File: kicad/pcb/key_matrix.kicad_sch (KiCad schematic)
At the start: 47 parts, among them SW1 EC_SW

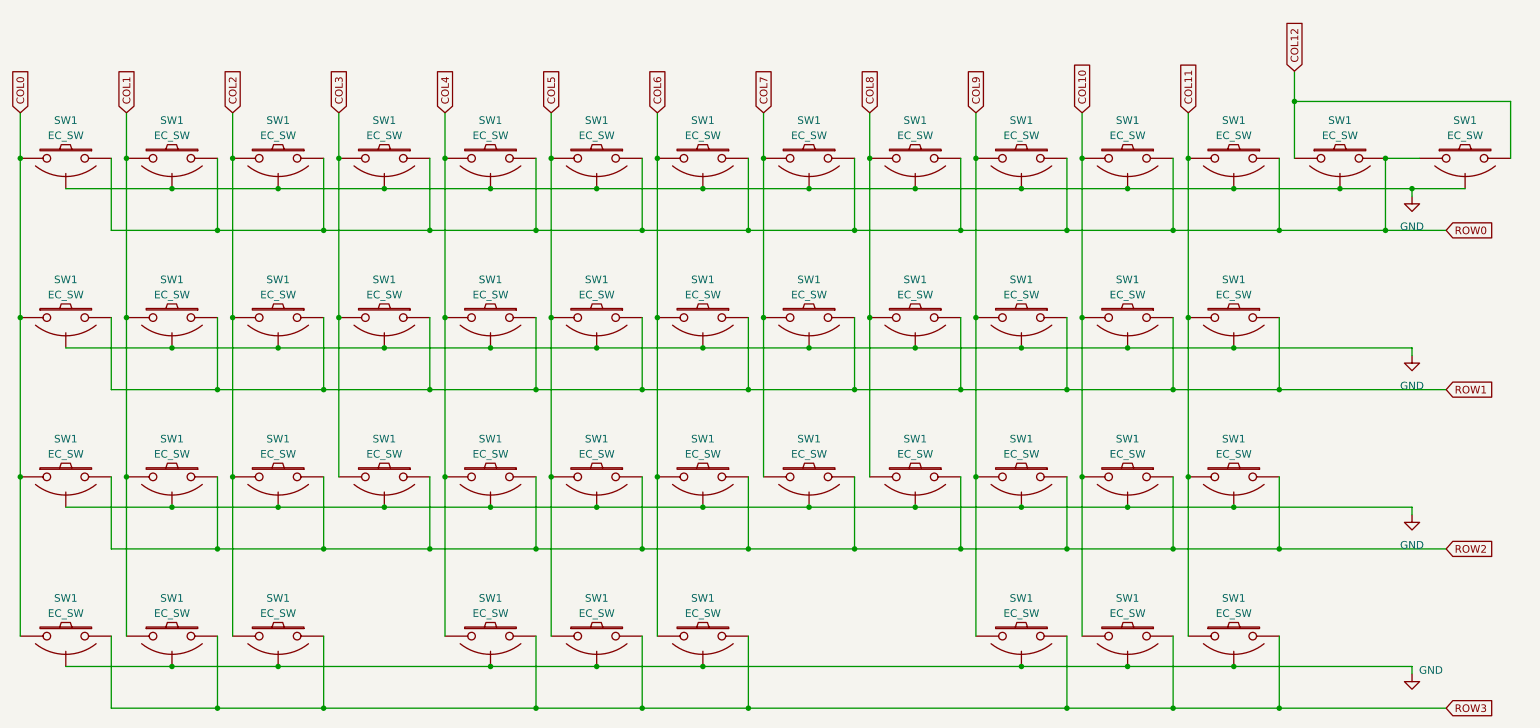
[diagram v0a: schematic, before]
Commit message: should be ok for proto order
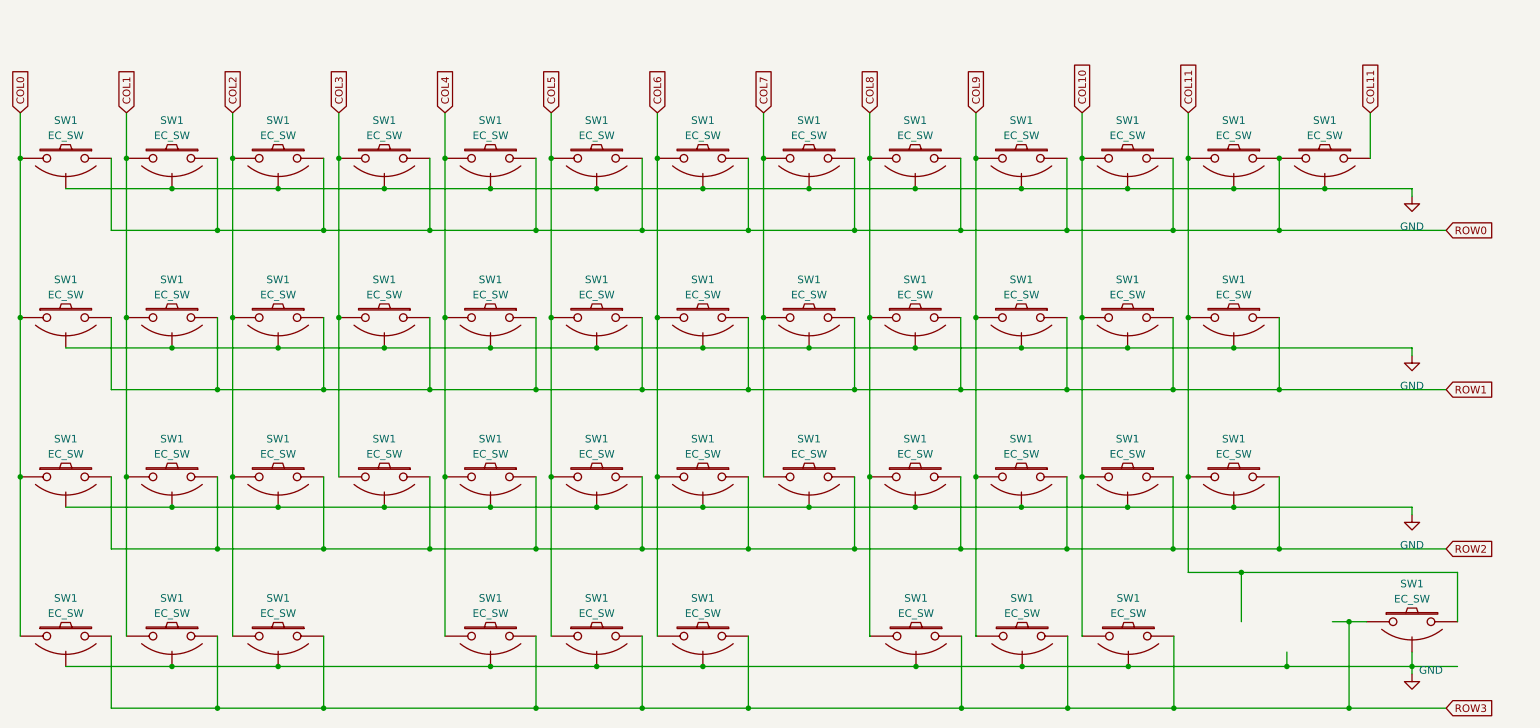
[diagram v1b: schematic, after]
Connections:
- net COL12 is gone; now on net COL11: SW1.1, SW1.2
- net COL0: now also SW1.1; no longer SW1.2
- net COL1: now also SW1.2; no longer SW1.1
- net COL10: now also SW1.2; no longer SW1.2
- net COL11: no longer SW1.1
- net COL4: now also SW1.2; no longer SW1.1
- net COL8: now also SW1.1, SW1.1, SW1.2; no longer SW1.2, SW1.2
- net COL9: now also SW1.1; no longer SW1.2
- net ROW0: no longer SW1.1
- net ROW1: now also SW1.2; no longer SW1.1
- net ROW2: now also SW1.2; no longer SW1.1
- net ROW3: now also SW1.1, SW1.1, SW1.1, SW1.1, SW1.2, SW1.2; no longer SW1.1, SW1.1, SW1.2, SW1.2, SW1.2
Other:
- moved on the sheet: SW1

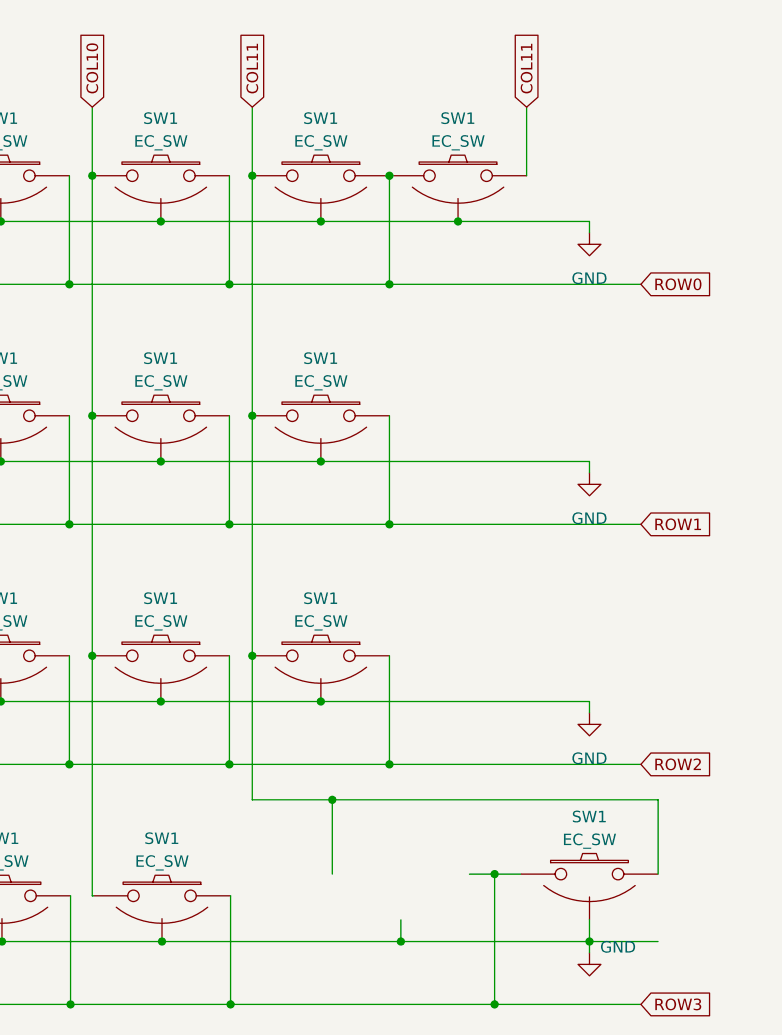
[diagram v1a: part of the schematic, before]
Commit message: adding right shift option
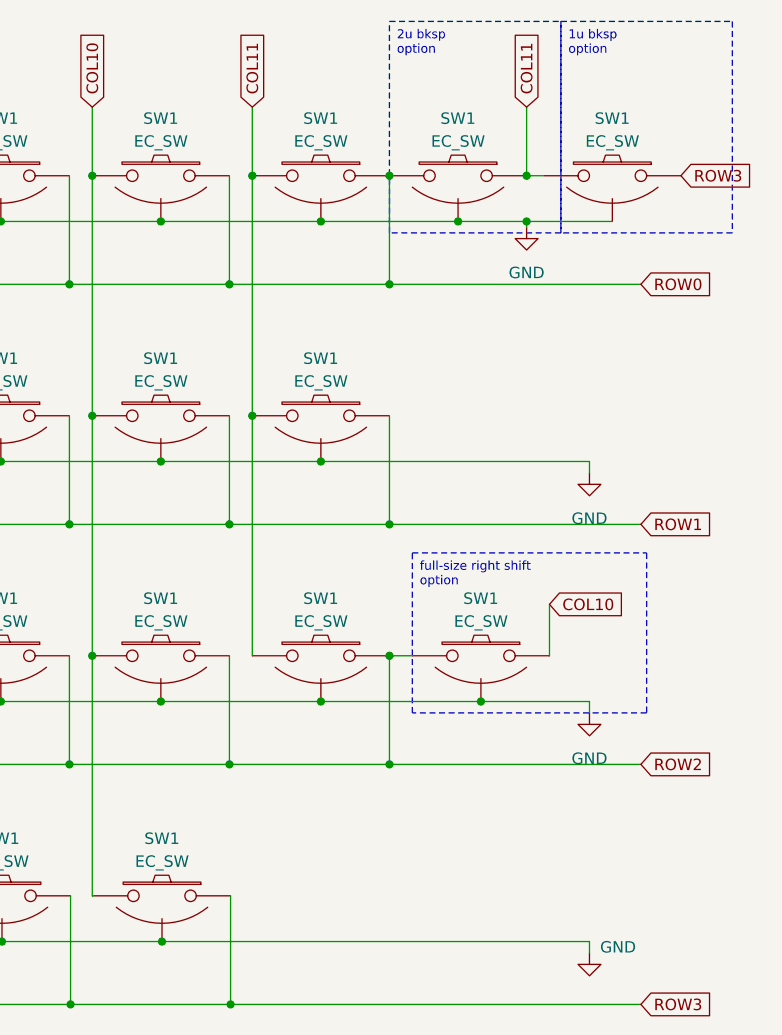
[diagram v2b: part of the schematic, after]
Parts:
- added SW1: EC_SW, capacitive_sensors:capy_pad_1U, symbol cipulot_parts:EC_SW
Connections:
- net COL10: now also SW1.1
- net GND: now also SW1.3 (SG)
- net ROW2: now also SW1.2
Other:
- moved on the sheet: SW1
